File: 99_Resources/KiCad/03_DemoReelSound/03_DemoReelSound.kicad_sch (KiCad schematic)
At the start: 11 parts, among them J1 Conn_01x03_Pin, J4 Conn_01x03_Socket, U1 BlueToothAudioR

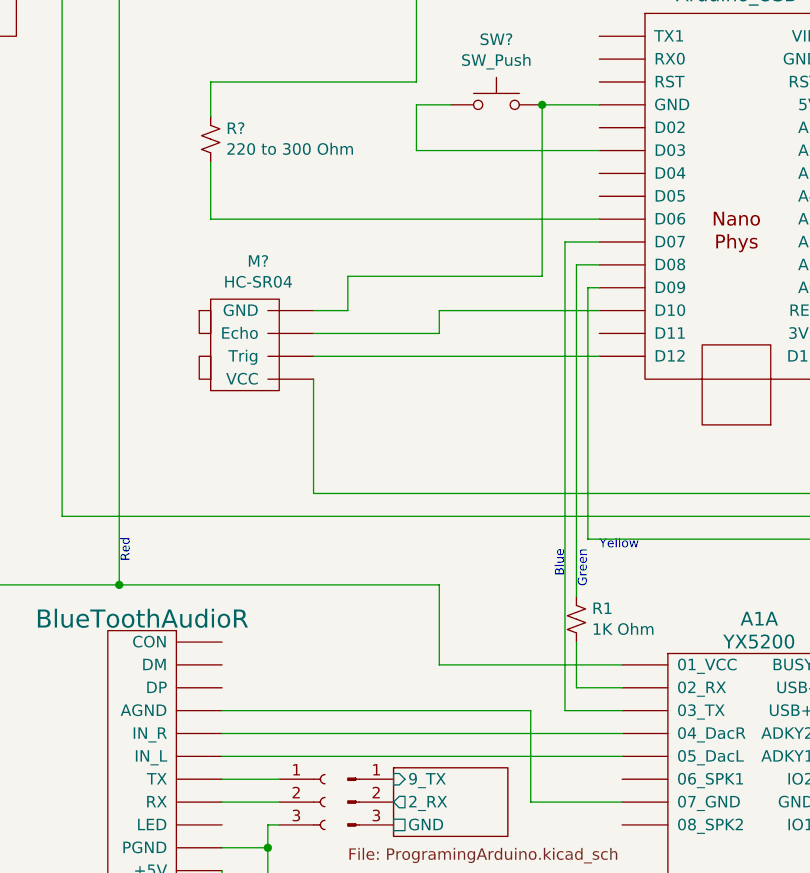
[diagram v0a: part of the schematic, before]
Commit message: make pin numbers consistent, more DemoReelSound work
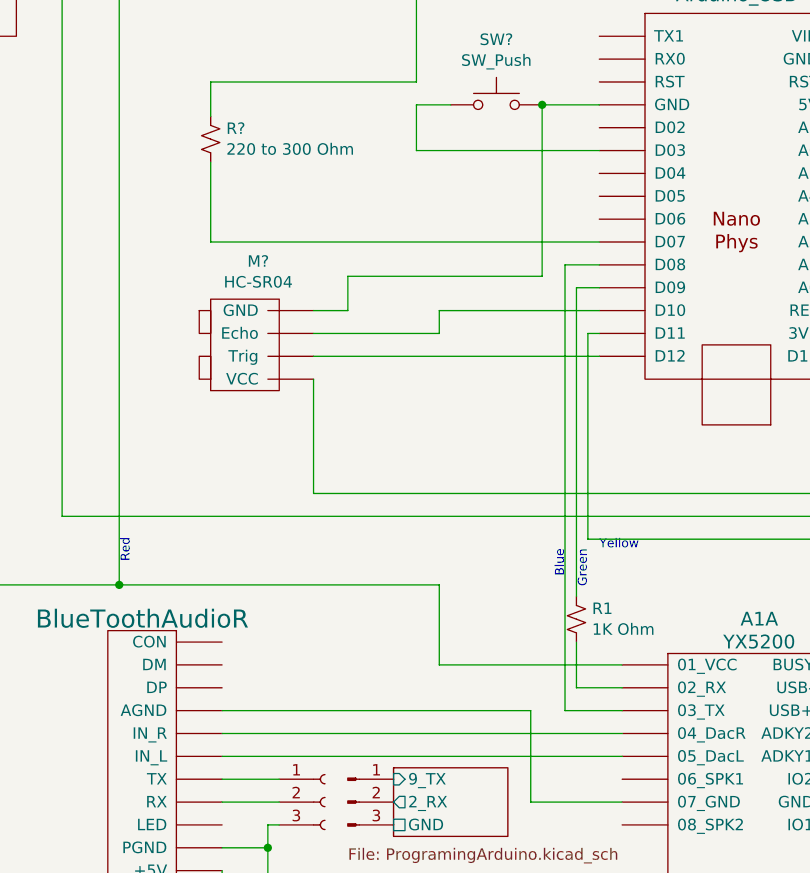
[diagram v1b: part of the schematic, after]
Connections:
- net at A?.~ (VIN): now also A1.~ (USB-_15)
- net at A1.~ (USB-_15): no longer A?.~ (VIN)
- net at Z?.~ (GND): now also A1.~ (USB-_15), U1.~ (TX)
- net at U1.~ (TX): now also J4.2 (Pin_2)
- new net: A?.~ (VIN), M?.~ (VCC), SW?.2
- new net: A?.~ (VIN), M?.~ (VCC) (x2)
- new net: A1.~ (USB-_15), A?.~ (VIN), J4.3 (Pin_3), U1.~ (TX), Z?.~ (GND)
- new net: A1.~ (USB-_15), A?.~ (VIN)
- new net: A1.~ (USB-_15), U1.~ (TX) (x3)
- now unconnected: A1.~ (USB-_15), A1.~ (USB-_15), A1.~ (USB-_15), A1.~ (USB-_15), A1.~ (USB-_15), A1.~ (USB-_15)
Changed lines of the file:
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@@
+    (stroke (width 0) (type default))
+  )
+  (wire (pts (xy 111.76 114.3) (xy 115.57 114.3))
     (stroke (width 0) (type default))
   )
@@
     (stroke (width 0) (type default))
   )
+  (wire (pts (xy 72.39 102.87) (xy 72.39 111.76))
+    (stroke (width 0) (type default))
+  )
   (wire (pts (xy 107.95 173.99) (xy 107.95 163.83))
     (stroke (width 0) (type default))
@@
     (stroke (width 0) (type default))
   )
-  (wire (pts (xy 114.3 116.84) (xy 114.3 144.78))
-    (stroke (width 0) (type default))
-  )
   (wire (pts (xy 78.74 179.07) (xy 73.66 179.07))
     (stroke (width 0) (type default))
   )
-  (wire (pts (xy 115.57 111.76) (xy 111.76 111.76))
-    (stroke (width 0) (type default))
-  )
   (wire (pts (xy 73.66 173.99) (xy 80.01 173.99))
     (stroke (width 0) (type default))
@@
     (stroke (width 0) (type default))
   )
-  (wire (pts (xy 115.57 114.3) (xy 113.03 114.3))
-    (stroke (width 0) (type default))
-  )
   (wire (pts (xy 118.11 158.75) (xy 97.79 158.75))
     (stroke (width 0) (type default))
@@
     (stroke (width 0) (type default))
   )
+  (wire (pts (xy 115.57 111.76) (xy 72.39 111.76))
+    (stroke (width 0) (type default))
+  )
   (wire (pts (xy 115.57 124.46) (xy 83.82 124.46))
     (stroke (width 0) (type default))
@@
     (stroke (width 0) (type default))
   )
-  (wire (pts (xy 115.57 116.84) (xy 114.3 116.84))
+  (wire (pts (xy 113.03 116.84) (xy 113.03 151.13))
     (stroke (width 0) (type default))
   )
@@
     (stroke (width 0) (type default))
   )
-  (wire (pts (xy 111.76 111.76) (xy 111.76 163.83))
+  (wire (pts (xy 114.3 121.92) (xy 115.57 121.92))
     (stroke (width 0) (type default))
   )
@@
     (stroke (width 0) (type default))
   )
-  (wire (pts (xy 72.39 102.87) (xy 72.39 109.22))
-    (stroke (width 0) (type default))
-  )
   (wire (pts (xy 62.23 73.66) (xy 92.71 73.66))
     (stroke (width 0) (type default))
@@
     (stroke (width 0) (type default))
   )
-  (wire (pts (xy 72.39 109.22) (xy 115.57 109.22))
+  (wire (pts (xy 113.03 116.84) (xy 115.57 116.84))
     (stroke (width 0) (type default))
   )
@@
     (stroke (width 0) (type default))
   )
-  (wire (pts (xy 113.03 114.3) (xy 113.03 151.13))
-    (stroke (width 0) (type default))
-  )
   (wire (pts (xy 73.66 171.45) (xy 80.01 171.45))
     (stroke (width 0) (type default))
@@
     (stroke (width 0) (type default))
   )
+  (wire (pts (xy 111.76 114.3) (xy 111.76 163.83))
+    (stroke (width 0) (type default))
+  )
   (wire (pts (xy 154.94 173.99) (xy 148.59 173.99))
     (stroke (width 0) (type default))
   )
+  (wire (pts (xy 114.3 121.92) (xy 114.3 144.78))
+    (stroke (width 0) (type default))
+  )
